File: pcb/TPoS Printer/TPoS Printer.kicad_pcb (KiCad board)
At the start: 2 copper layers, 48.9 x 28.6 mm, 4 parts

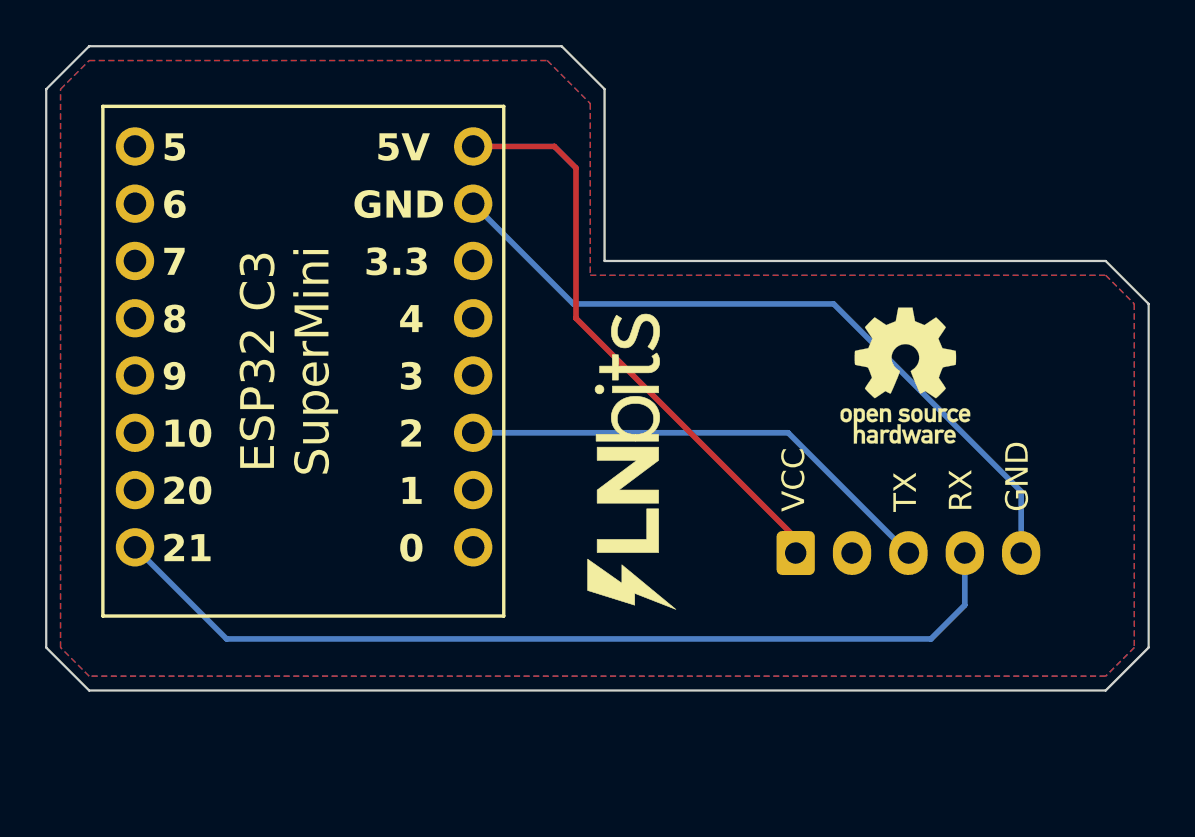
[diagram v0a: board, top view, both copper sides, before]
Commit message: Updated KiCad with square board and mounting holes
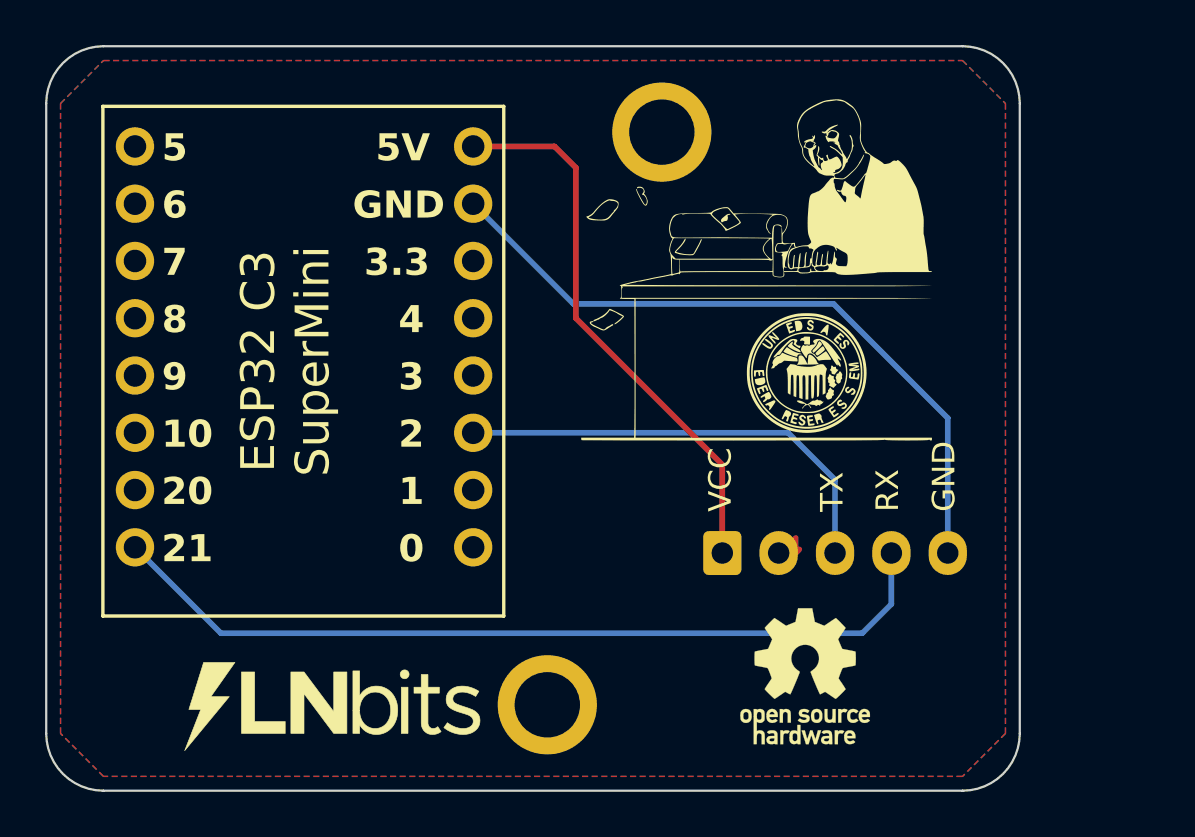
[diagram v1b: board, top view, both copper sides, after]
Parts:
- added REF**: M2.5, Connector_PinHeader_1.00mm:PinHeader_1x01_P1.00mm_Vertical, F.Cu at (86.4, 74.3)
- added REF**: M2.5, Connector_PinHeader_1.00mm:PinHeader_1x01_P1.00mm_Vertical, F.Cu at (91.4, 48.9)
- moved REF** 14.1 mm to (97.8, 73.0)
- moved JST_XH_B5B-XH-A_1x05 3.26 mm to (94.1, 67.6)
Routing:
- net (no net): track 121.6 -> 114.7 mm
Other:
- board size 48.9 x 28.6 mm -> 43.2 x 33 mm
